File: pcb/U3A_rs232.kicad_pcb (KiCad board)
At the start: 2 copper layers, 34.5 x 26.4 mm, 16 parts, among them J1 Conn_02x05_Odd_Even, J2 Conn_01x07_Socket, J4 Conn_01x08_Socket, U1 MAX3232

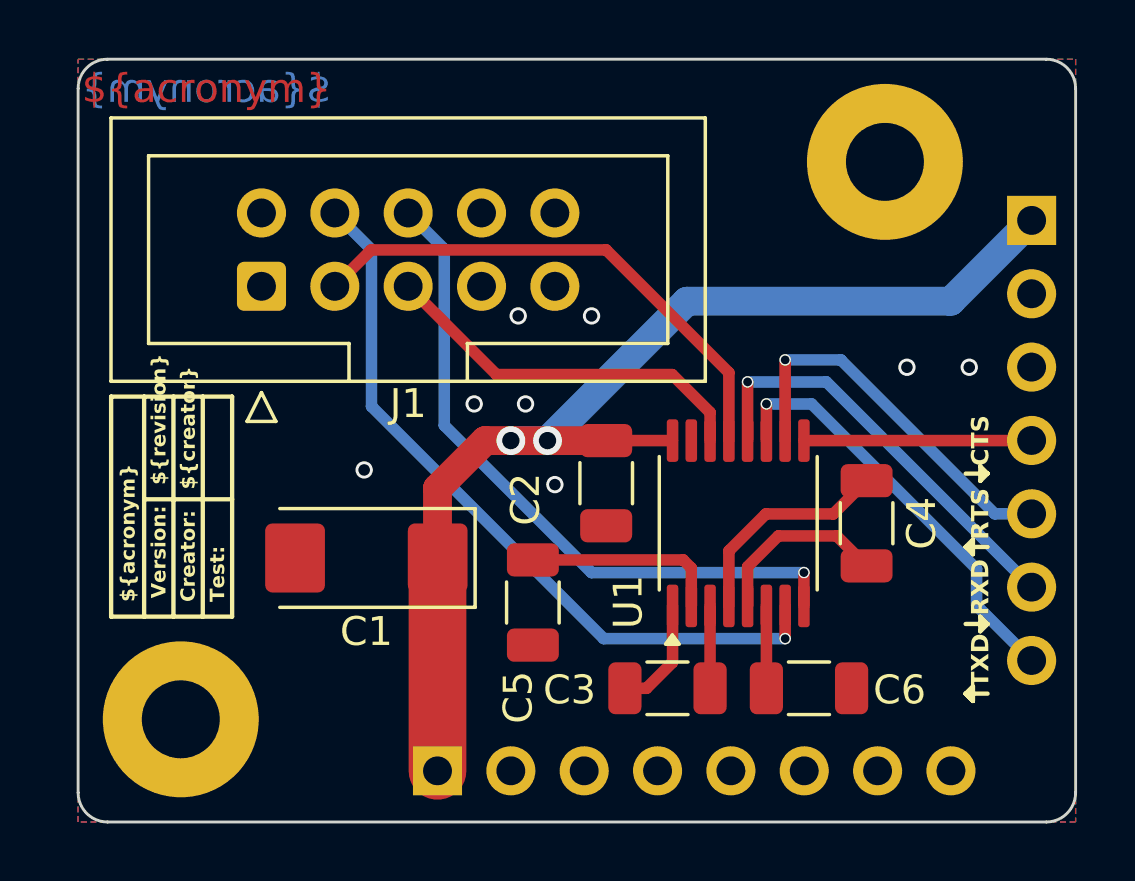
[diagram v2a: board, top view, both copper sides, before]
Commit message: Rearrange rs232 traces
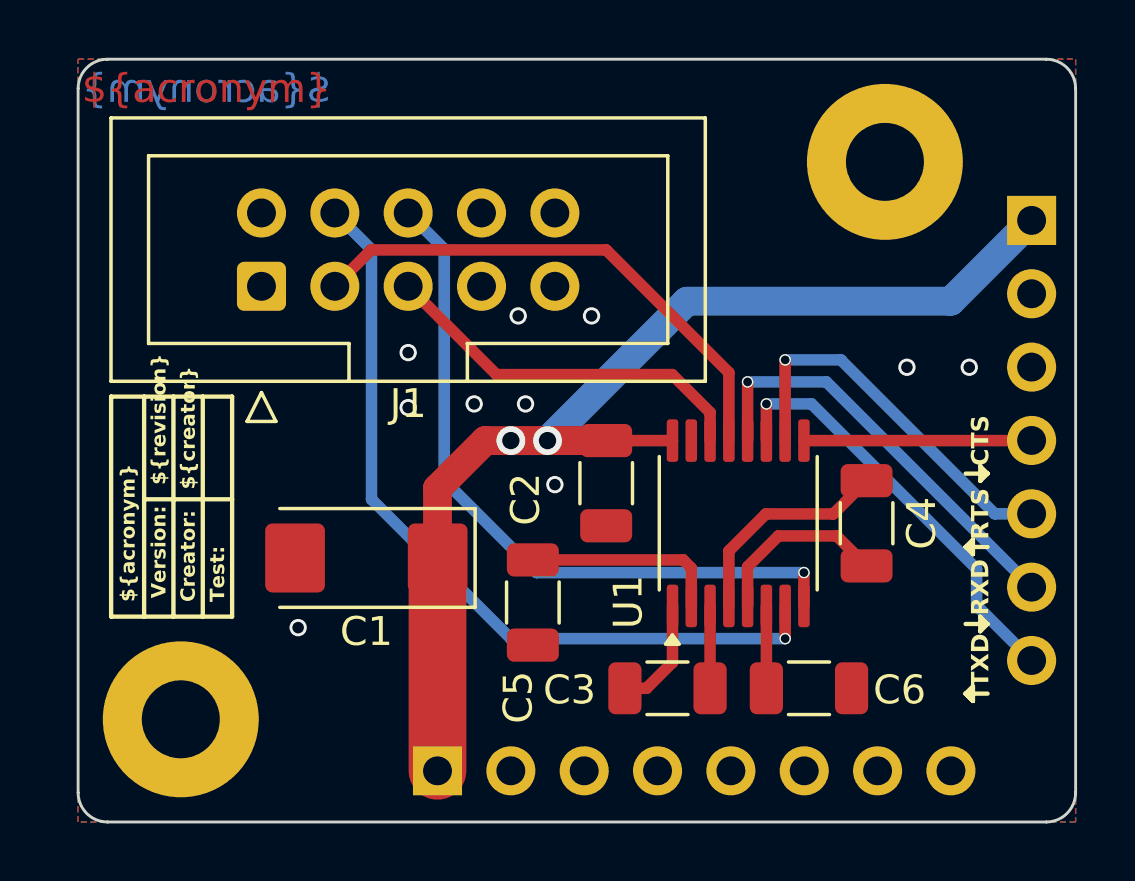
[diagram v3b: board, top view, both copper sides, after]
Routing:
- net Net-(J1-Pin_4): track 26.0 -> 27.9 mm
- net Net-(J1-Pin_6): track 23.6 -> 24.7 mm
- net GND: vias 8 -> 10
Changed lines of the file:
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@@
+	)
+	(via
+		(at 152.4 95.885)
+		(size 0.6)
+		(drill 0.4)
+		(layers "F.Cu" "B.Cu")
+		(free yes)
+		(net 1)
 	)
 	(via
@@
 	)
 	(via
-		(at 154.686 90.424)
-		(size 0.6)
-		(drill 0.4)
-		(layers "F.Cu" "B.Cu")
-		(free yes)
-		(net 1)
-	)
-	(via
 		(at 161.29 90.932)
+		(size 0.6)
+		(drill 0.4)
+		(layers "F.Cu" "B.Cu")
+		(free yes)
+		(net 1)
+	)
+	(via
+		(at 156.21 86.36)
+		(size 0.6)
+		(drill 0.4)
+		(layers "F.Cu" "B.Cu")
+		(free yes)
+		(net 1)
+	)
+	(via
+		(at 156.21 88.265)
 		(size 0.6)
 		(drill 0.4)
@@
 	)
 	(segment
-		(start 169.915 93.98)
-		(end 162.56 93.98)
-		(width 0.4)
-		(layer "B.Cu")
-		(net 25)
-	)
-	(segment
-		(start 162.56 93.98)
-		(end 157.46 88.88)
-		(width 0.4)
-		(layer "B.Cu")
-		(net 25)
-	)
-	(segment
 		(start 157.46 82.7745)
 		(end 156.21 81.5245)
@@
 	)
 	(segment
-		(start 157.46 88.88)
+		(start 169.915 93.98)
+		(end 160.655 93.98)
+		(width 0.4)
+		(layer "B.Cu")
+		(net 25)
+	)
+	(segment
+		(start 160.655 93.98)
+		(end 157.46 90.785)
+		(width 0.4)
+		(layer "B.Cu")
+		(net 25)
+	)
+	(segment
+		(start 157.46 90.785)
 		(end 157.46 82.7745)
 		(width 0.4)
@@
 	)
 	(segment
+		(start 159.766 96.266)
+		(end 154.94 91.44)
+		(width 0.4)
+		(layer "B.Cu")
+		(net 27)
+	)
+	(segment
 		(start 169.265 96.266)
-		(end 162.981472 96.266)
-		(width 0.4)
-		(layer "B.Cu")
-		(net 27)
-	)
-	(segment
-		(start 162.981472 96.266)
-		(end 154.94 88.224528)
+		(end 159.766 96.266)
 		(width 0.4)
 		(layer "B.Cu")
@@
 	)
 	(segment
-		(start 154.94 88.224528)
+		(start 154.94 91.44)
 		(end 154.94 82.7945)
 		(width 0.4)
